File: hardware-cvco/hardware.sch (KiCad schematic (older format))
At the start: 164 parts, among them J1 SMA, J2 SMA, J3 SMA, J4 SMA, J5 SMA, J6 SMA, J7 SMA, J8 Pickit 2, J9 DC, Q1 AOD403, Q2 MBT2222, SW1 On/Off, U1 74LS07, U10 TPS61046, U11 LM358, U12 LM317DCYR, U13 MCP73871-2AA, U14 LM386, U2 NLB-310-T1, U3 NLB-310-T1, U4 NLB-310-T1, U5 NLB-310-T1, U6 PIC12F675-ISN, U7 NLB-310-T1, U8 NLB-310-T1, U9 NLB-310-T1, Y1 CVCO55CW-0100-0200, Y2 CVCO55CW-0200-0500, Y3 CV55CW500-1000, Y4 CVCO55CW-1000-2000, Y5 CV55BE1600-3200, Y6 CVCO55CC-3180-3710, Y7 CVCO55CW-3500-4500

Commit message: Added icons & icon footprints - CVCO.
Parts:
- removed C44: 10μF, Capacitor_SMD:C_0805_2012Metric_Pad1.15x1.40mm_HandSolder, symbol Device:C
- removed C49, C50: 4.7μF, Capacitor_SMD:C_0805_2012Metric_Pad1.15x1.40mm_HandSolder, symbol Device:C
- removed D10: Yellow, CVCO:2-2.54mm-Horizontal-Molex, symbol Device:LED
- removed R37: 120, Resistor_SMD:R_0805_2012Metric_Pad1.15x1.40mm_HandSolder, symbol Device:R
- removed R47, R49: 10k, Resistor_SMD:R_0805_2012Metric_Pad1.15x1.40mm_HandSolder, symbol Device:R
- removed R48: 1k, Resistor_SMD:R_0805_2012Metric_Pad1.15x1.40mm_HandSolder, symbol Device:R
- removed U13: MCP73871-2AA, Package_DFN_QFN:QFN-20-1EP_4x4mm_P0.5mm_EP2.5x2.5mm, symbol Battery_Management:MCP73871-2AA
- added C45, C46: 1μF, Capacitor_SMD:C_0805_2012Metric_Pad1.15x1.40mm_HandSolder, symbol Device:C
- added TH1: 10k, CVCO:2-2.54mm-Horizontal-Molex, symbol Device:Thermistor_NTC
- added U11: BQ21040, Package_TO_SOT_SMD:SOT-23-6, symbol CVCO:BQ21040
- D9: value Red -> Orange
- R33: value 10k -> 15k; LCSC Part # C55866 -> (none)
- renumbered C45 to C44, C46 to C47, C47 to C48, C48 to C49, C51 to C50, C52 to C51, C53 to C52, C54 to C53, C55 to C54, C56 to C55, C57 to C56, C58 to C57, C59 to C58, D11 to D10, D12 to D11, D13 to D12, R39 to R34, R34 to R35, R38 to R36, R35 to R37, R36 to R38, R40 to R39, R41 to R40, R42 to R41, R43 to R42, R44 to R43, R45 to R44, R46 to R45, R50 to R46, R51 to R47, R52 to R48, R53 to R49, R54 to R50, R55 to R51, R56 to R52, U11 to U12, U12 to U13
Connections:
- wire segments 582 -> 553
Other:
- moved on the sheet: BT1, C44, C47, C48, C49, C50, C53, C54, C55, C56, C58, D12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

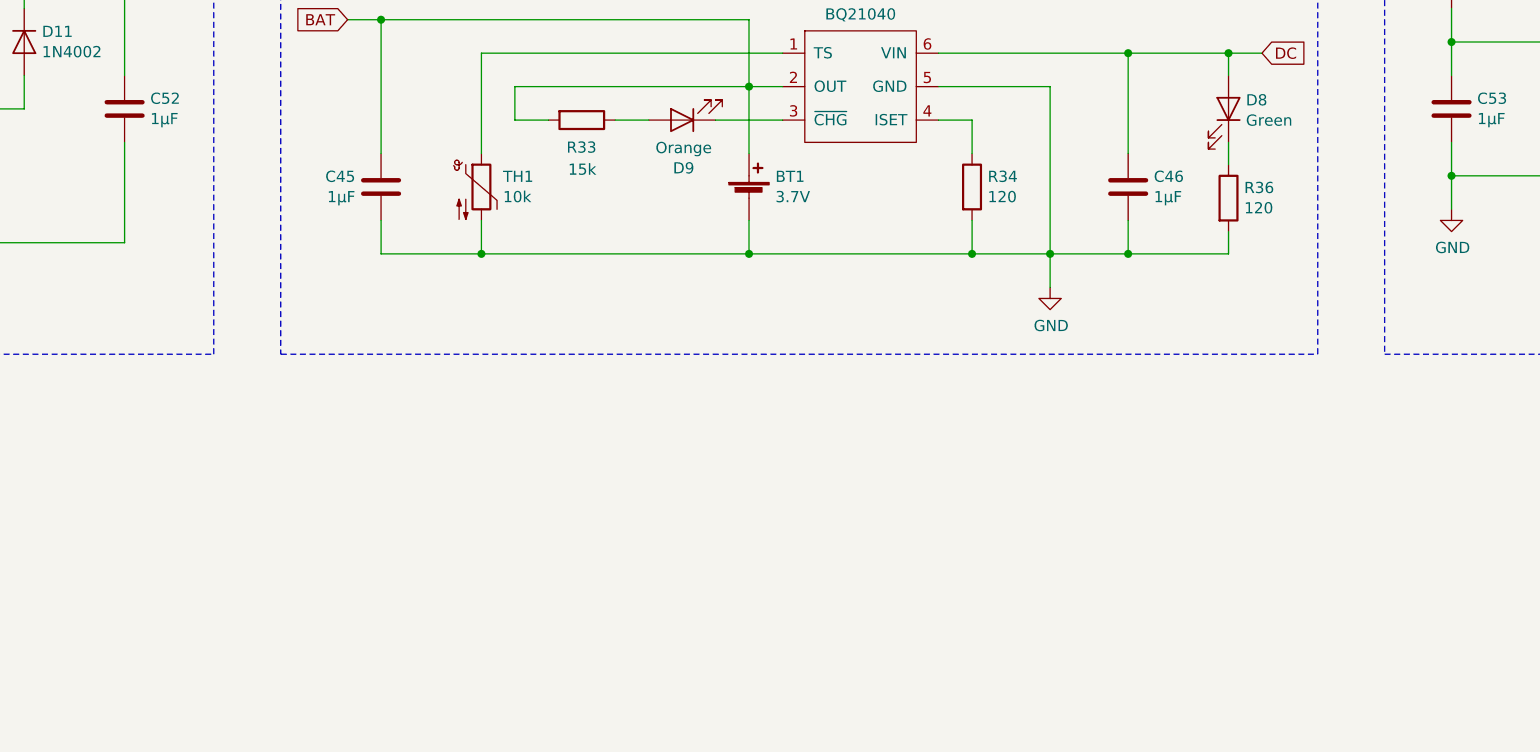
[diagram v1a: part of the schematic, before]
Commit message: Assigned LCSC parts to battery mng. section.
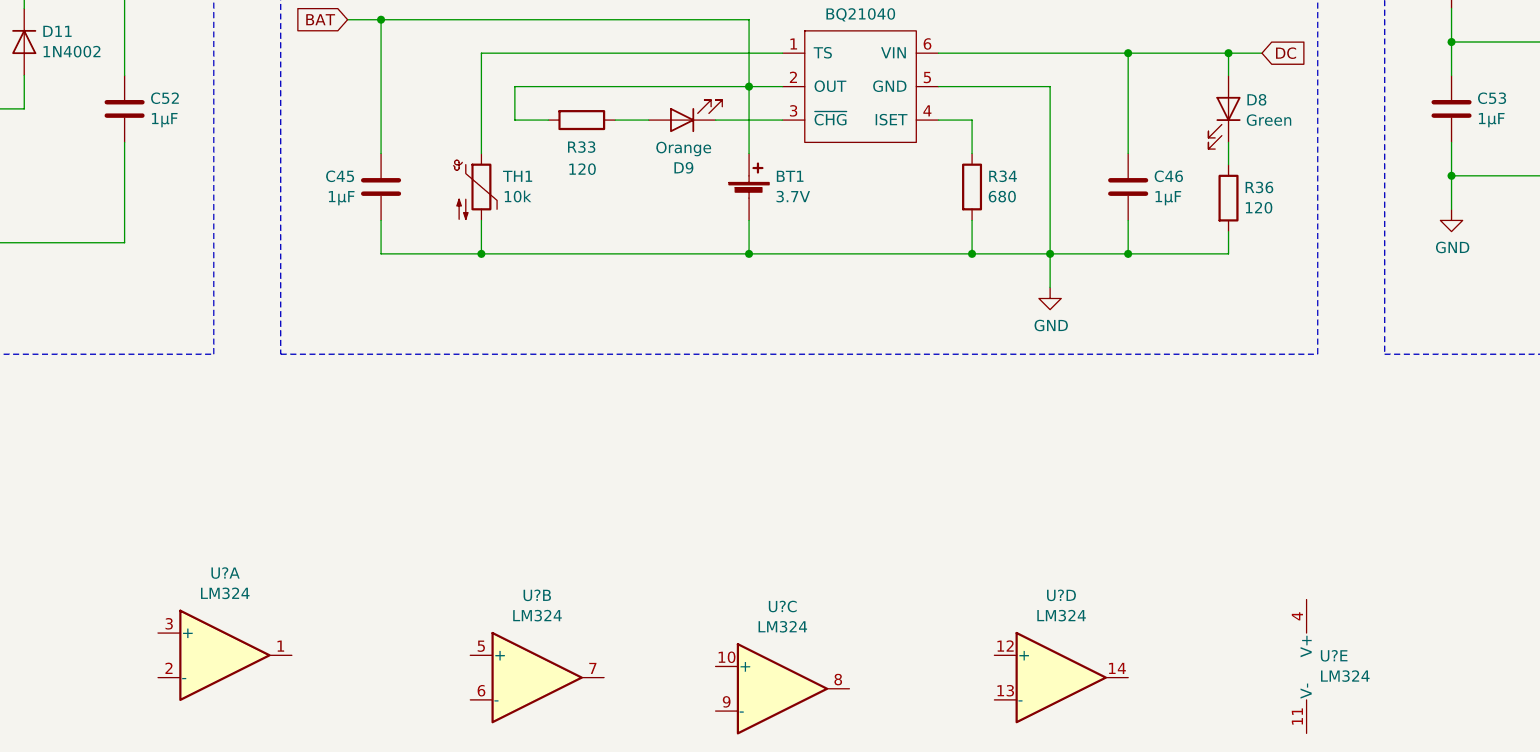
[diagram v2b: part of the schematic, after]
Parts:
- added U? (x5): LM324, Package_SO:SOIC-14_3.9x8.7mm_P1.27mm, symbol Amplifier_Operational:LM324
- D8: LCSC Part # (none) -> C99763
- D9: LCSC Part # (none) -> C99759
- R33: value 15k -> 120; LCSC Part # (none) -> C111022
- R34: value 120 -> 680; LCSC Part # C111022 -> C17798
- TH1: LCSC Part # (none) -> C13879
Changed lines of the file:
@@
 P 8450 13050
 F 0 "R34" H 8520 13096 50  0000 L CNN
-F 1 "120" H 8520 13005 50  0000 L CNN
+F 1 "680" H 8520 13005 50  0000 L CNN
 F 2 "Resistor_SMD:R_0805_2012Metric_Pad1.15x1.40mm_HandSolder" V 8380 13050 50  0001 C CNN
 F 3 "~" H 8450 13050 50  0001 C CNN
-F 4 "C111022" H 8450 13050 50  0001 C CNN "LCSC Part #"
+F 4 "C17798" H 8450 13050 50  0001 C CNN "LCSC Part #"
 	1    8450 13050
 	1    0    0    -1
@@
 F 2 "CVCO:2-2.54mm-Horizontal-Molex" H 9600 12700 50  0001 C CNN
 F 3 "~" H 9600 12700 50  0001 C CNN
+F 4 "C99763" V 9600 12700 50  0001 C CNN "LCSC Part #"
 	1    9600 12700
 	0    1    -1   0
@@
 F 2 "CVCO:2-2.54mm-Horizontal-Molex" H 6250 13100 50  0001 C CNN
 F 3 "~" H 6250 13100 50  0001 C CNN
+F 4 "C13879" H 6250 13050 50  0001 C CNN "LCSC Part #"
 	1    6250 13050
 	1    0    0    -1
@@
 F 2 "CVCO:2-2.54mm-Horizontal-Molex" H 7150 12750 50  0001 C CNN
 F 3 "~" H 7150 12750 50  0001 C CNN
+F 4 "C99759" H 7150 12750 50  0001 C CNN "LCSC Part #"
 	1    7150 12750
 	-1   0    0    1
@@
 P 6700 12750
 F 0 "R33" V 6823 12749 50  0000 C CNN
-F 1 "15k" V 6922 12752 50  0000 C CNN
+F 1 "120" V 6922 12752 50  0000 C CNN
 F 2 "Resistor_SMD:R_0805_2012Metric_Pad1.15x1.40mm_HandSolder" V 6630 12750 50  0001 C CNN
 F 3 "~" H 6700 12750 50  0001 C CNN
+F 4 "C111022" V 6700 12750 50  0001 C CNN "LCSC Part #"
 	1    6700 12750
 	0    1    1    0
@@
 Wire Wire Line
 	8800 13500 8800 13350
+$Comp
+L Amplifier_Operational:LM324 U?
+U 1 1 64668408
+P 5100 15150
+F 0 "U?" H 5100 15517 50  0000 C CNN
+F 1 "LM324" H 5100 15426 50  0000 C CNN
+F 2 "Package_SO:SOIC-14_3.9x8.7mm_P1.27mm" H 5050 15250 50  0001 C CNN
+F 3 "http://www.ti.com/lit/ds/symlink/lm2902-n.pdf" H 5150 15350 50  0001 C CNN
+F 4 "C71035" H 5100 15150 50  0001 C CNN "LCSC Part #"
+	1    5100 15150
+	1    0    0    -1
+$EndComp
+$Comp
+L Amplifier_Operational:LM324 U?
+U 2 1 64669F1A
+P 6500 15250
+F 0 "U?" H 6500 15617 50  0000 C CNN
+F 1 "LM324" H 6500 15526 50  0000 C CNN
+F 2 "Package_SO:SOIC-14_3.9x8.7mm_P1.27mm" H 6450 15350 50  0001 C CNN
+F 3 "http://www.ti.com/lit/ds/symlink/lm2902-n.pdf" H 6550 15450 50  0001 C CNN
+	2    6500 15250
+	1    0    0    -1
+$EndComp
+$Comp
+L Amplifier_Operational:LM324 U?
+U 3 1 6466BCFC
+P 7600 15300
+F 0 "U?" H 7600 15667 50  0000 C CNN
+F 1 "LM324" H 7600 15576 50  0000 C CNN
+F 2 "Package_SO:SOIC-14_3.9x8.7mm_P1.27mm" H 7550 15400 50  0001 C CNN
+F 3 "http://www.ti.com/lit/ds/symlink/lm2902-n.pdf" H 7650 15500 50  0001 C CNN
+	3    7600 15300
+	1    0    0    -1
+$EndComp
+$Comp
+L Amplifier_Operational:LM324 U?
+U 4 1 6466DD12
+P 8850 15250
+F 0 "U?" H 8850 15617 50  0000 C CNN
+F 1 "LM324" H 8850 15526 50  0000 C CNN
+F 2 "Package_SO:SOIC-14_3.9x8.7mm_P1.27mm" H 8800 15350 50  0001 C CNN
+F 3 "http://www.ti.com/lit/ds/symlink/lm2902-n.pdf" H 8900 15450 50  0001 C CNN
+	4    8850 15250
+	1    0    0    -1
+$EndComp
+$Comp
+L Amplifier_Operational:LM324 U?
+U 5 1 6466F95F
+P 10050 15200
+F 0 "U?" H 10008 15246 50  0000 L CNN
+F 1 "LM324" H 10008 15155 50  0000 L CNN
+F 2 "Package_SO:SOIC-14_3.9x8.7mm_P1.27mm" H 10000 15300 50  0001 C CNN
+F 3 "http://www.ti.com/lit/ds/symlink/lm2902-n.pdf" H 10100 15400 50  0001 C CNN
+	5    10050 15200
+	1    0    0    -1
+$EndComp
 $EndSCHEMATC

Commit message: Replaced LM358 with LM324.
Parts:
- removed U12: LM358, Package_SO:SO-8_5.3x6.2mm_P1.27mm, symbol Amplifier_Operational:LM358
- added R? (x2): 2k, Resistor_SMD:R_0805_2012Metric_Pad1.15x1.40mm_HandSolder, symbol Device:R
- R17: value 100 -> 1k; LCSC Part # C17408 -> C17513
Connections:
- net GND: now also U?.11 (V-), R?.2
- net P2_VDD: now also U?.12 (+), U?.4 (V+)
- net Sweep: now also U?.7
- net Tuner: now also U?.8, R?.1; no longer R17.1, R18.1
- net VGND: now also U?.2 (-)
- net at U?.1: now also R37.2, R41.1
- net at U?.3 (+): now also R41.2, R47.2
- net at U?.5 (+): now also C44.2, R37.1
- net at U?.6 (-): now also R51.1, R52.2
- net at U?.10 (+): now also R17.1, R18.1
- net at U?.9 (-): now also R?.1, R?.2
- net at U?.13 (-): now also U?.14
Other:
- note added: "Unused Op-Amp"
- moved on the sheet: C13, C22, R17, R18, U?A, U?B, U?C, U?D, U?E

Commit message: Non-RF section layout finished - CVCO.
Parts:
- C47, C48, C50, C54, C55, C56: symbol Device:C_Small -> Device:C
- R35, R39, R40, R44, R45, R50: symbol Device:R_Small -> Device:R
- gave numbers to parts that had none: 3
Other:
- moved on the sheet: C47, C48, C50, C54, C56, C58, D12, R35, R39, R40, R45, R50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

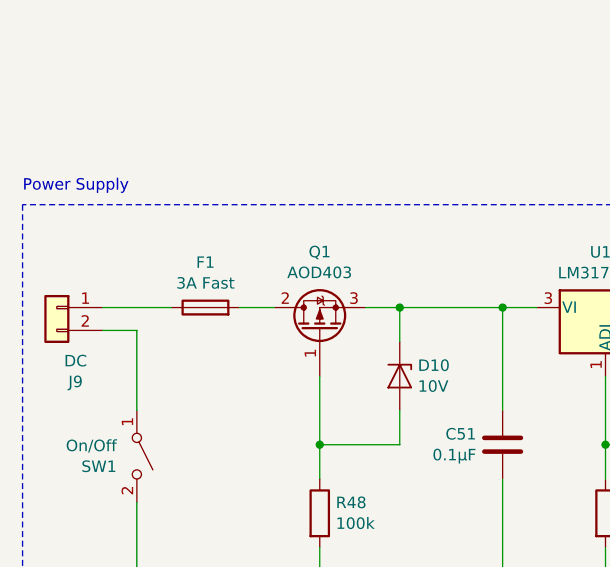
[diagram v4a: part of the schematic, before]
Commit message: Power Supply & Battery Management routing - CVCO.
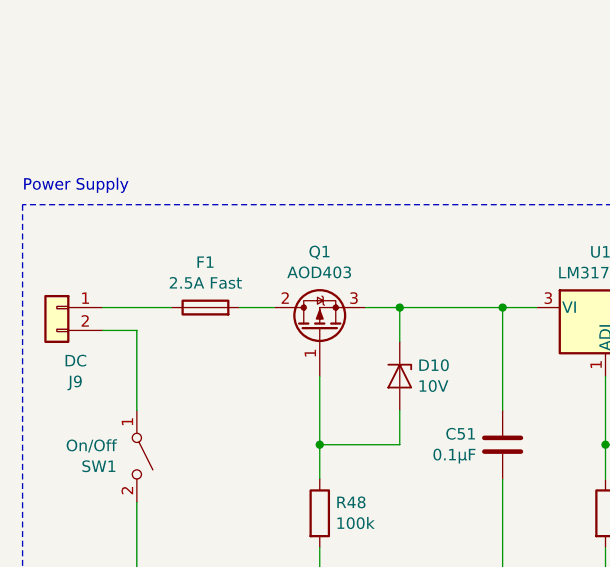
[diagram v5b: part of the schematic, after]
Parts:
- F1: value 3A Fast -> 2.5A Fast; LCSC Part # C163126 -> C163125
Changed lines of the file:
@@
 P 1550 12100
 F 0 "F1" V 1747 12100 50  0000 C CNN
-F 1 "3A Fast" V 1656 12100 50  0000 C CNN
+F 1 "2.5A Fast" V 1656 12100 50  0000 C CNN
 F 2 "Fuse:Fuse_1206_3216Metric_Pad1.42x1.75mm_HandSolder" V 1480 12100 50  0001 C CNN
 F 3 "~" H 1550 12100 50  0001 C CNN
-F 4 "C163126" V 1550 12100 50  0001 C CNN "LCSC Part #"
+F 4 "C163125" V 1550 12100 50  0001 C CNN "LCSC Part #"
 	1    1550 12100
 	0    -1   -1   0

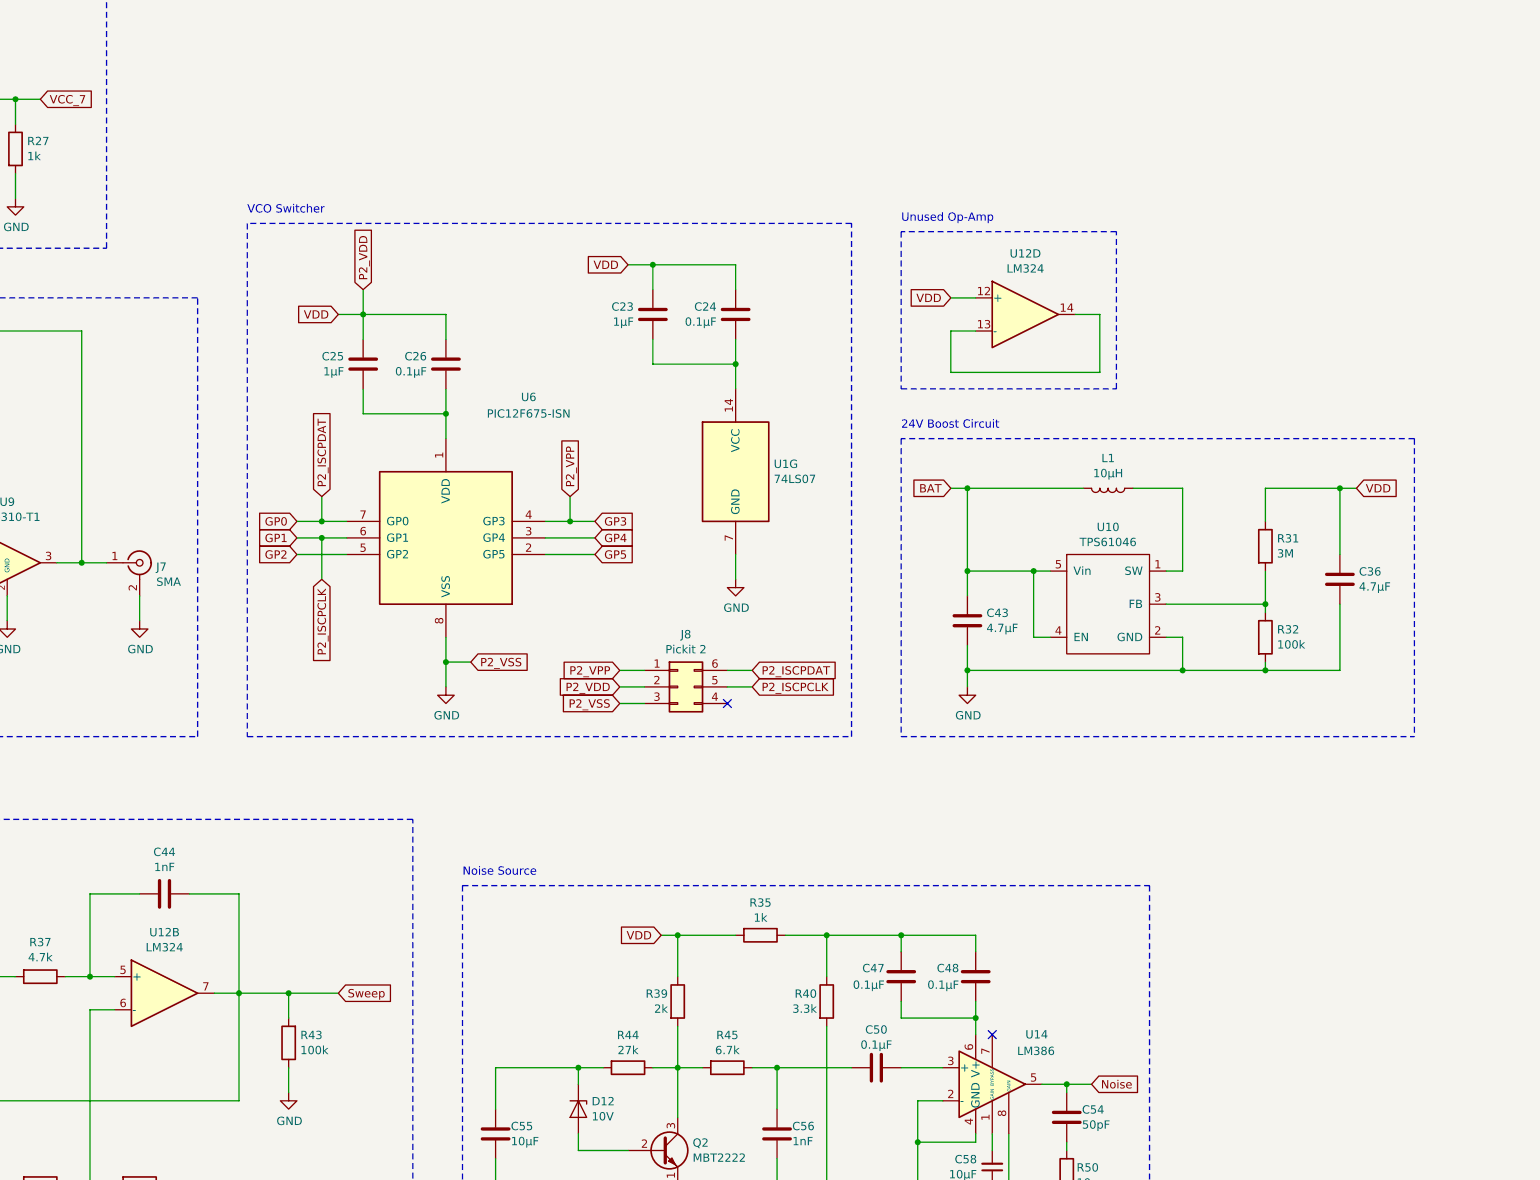
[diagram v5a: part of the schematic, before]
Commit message: Sweep Generator routing - CVCO.
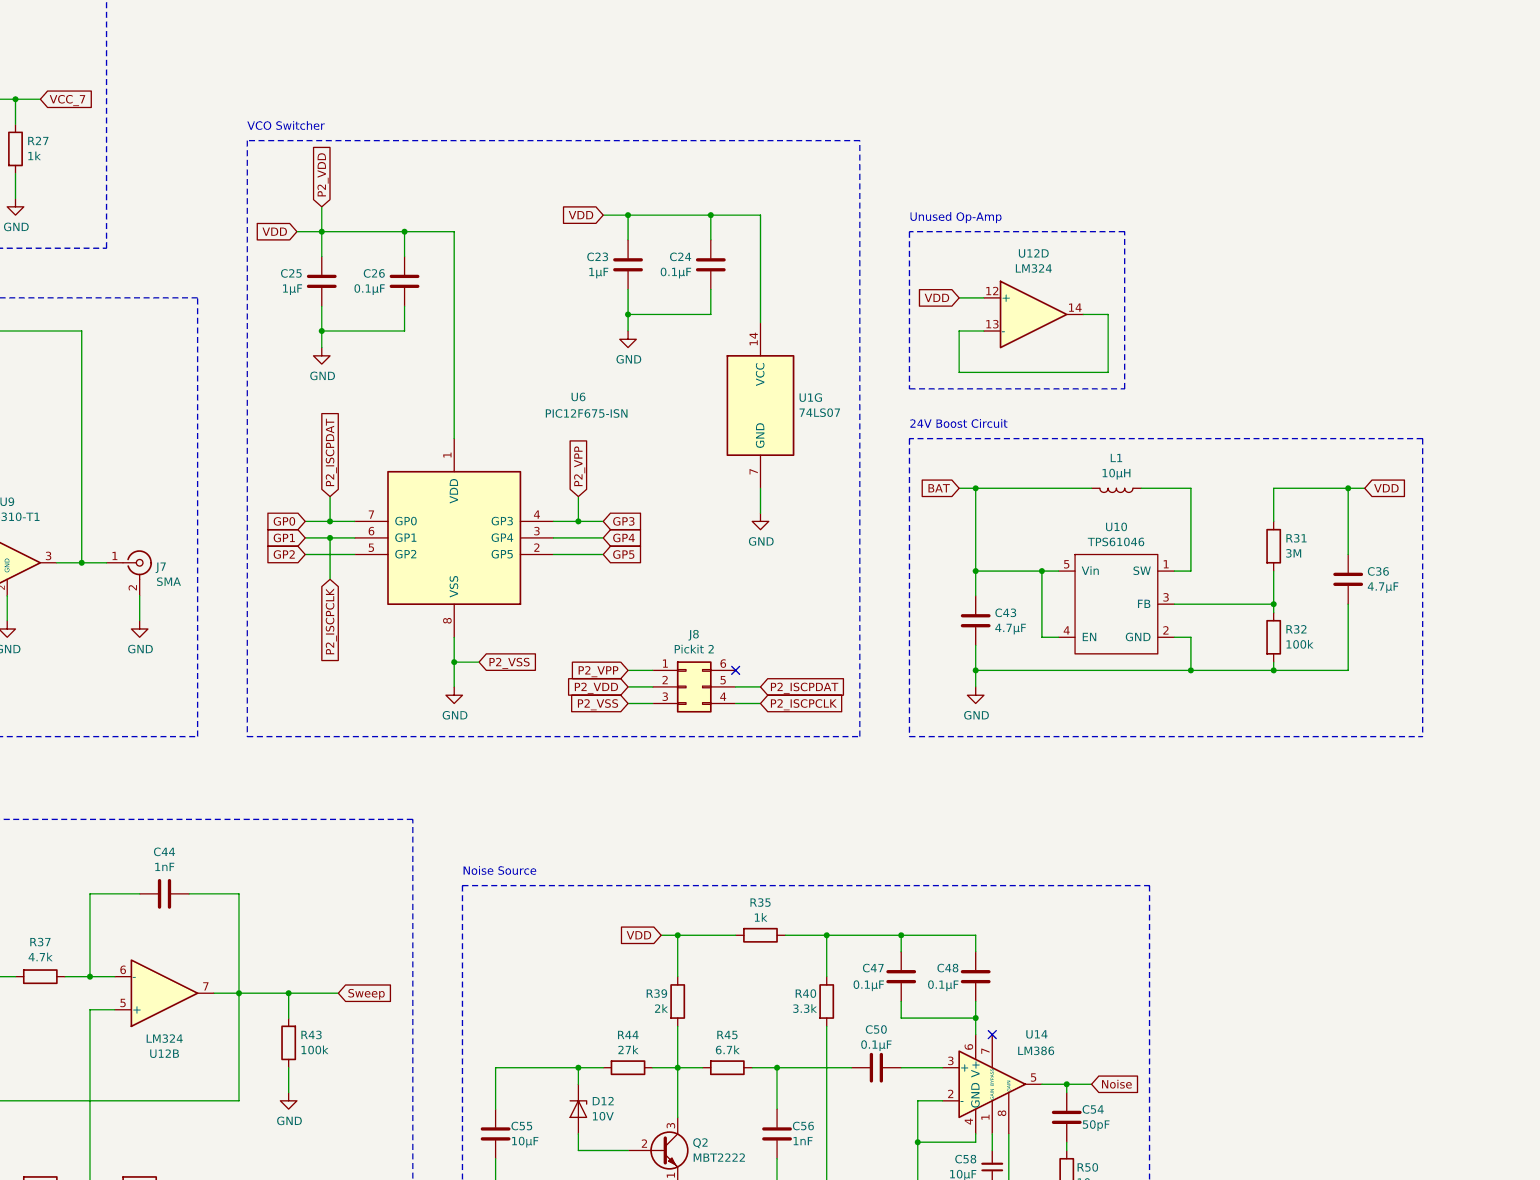
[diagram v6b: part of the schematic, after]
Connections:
- net GND: now also C23.2, C24.2, C25.2, C26.2
- net GP0: now also J8.5 (Pin_5); no longer J8.6 (Pin_6)
- net GP1: now also J8.4 (Pin_4); no longer J8.5 (Pin_5)
- net P2_VDD: now also U1.14 (VCC), U6.1 (VDD)
- net at C44.2, R37.1: now also U12.6 (-); no longer U12.5 (+)
- net at R51.1, R52.2: now also U12.5 (+); no longer U12.6 (-)
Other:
- moved on the sheet: C23, C24, C25, C26, C36, C43, J8, L1, R31, R32, U10, U12D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
